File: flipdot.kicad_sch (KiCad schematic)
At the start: 22 parts, among them J4 Conn_01x05_Pin, J8 Conn_01x05_Pin, Q1 FDN338P

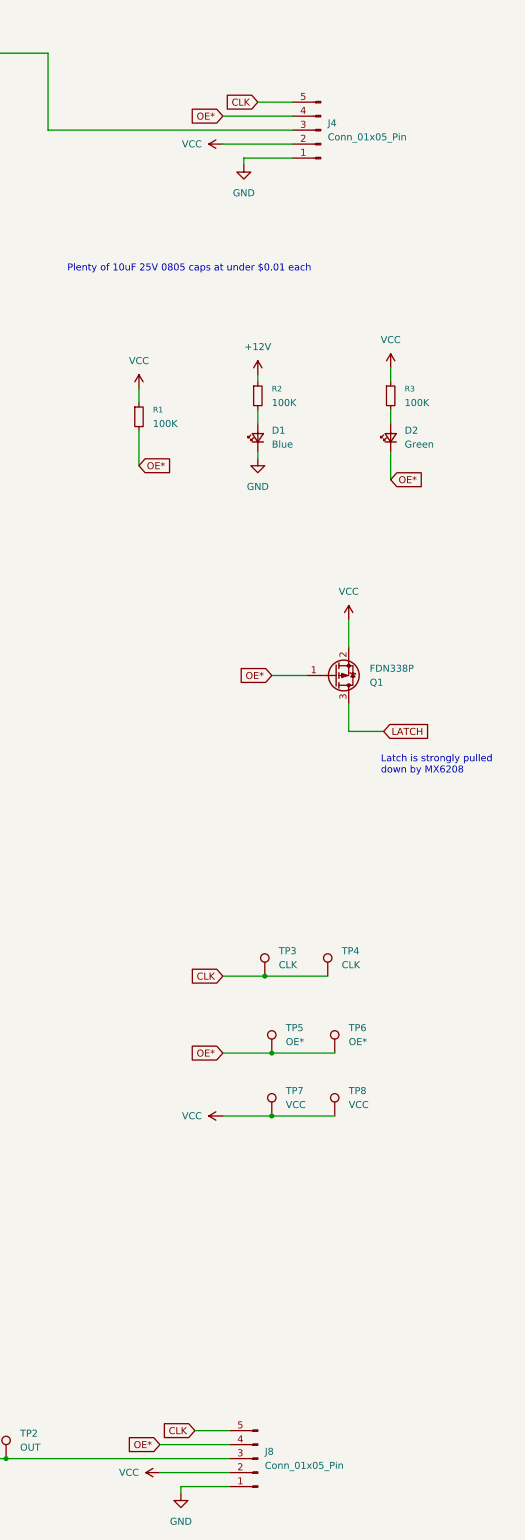
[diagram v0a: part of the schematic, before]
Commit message: add 12v out with polyfuse
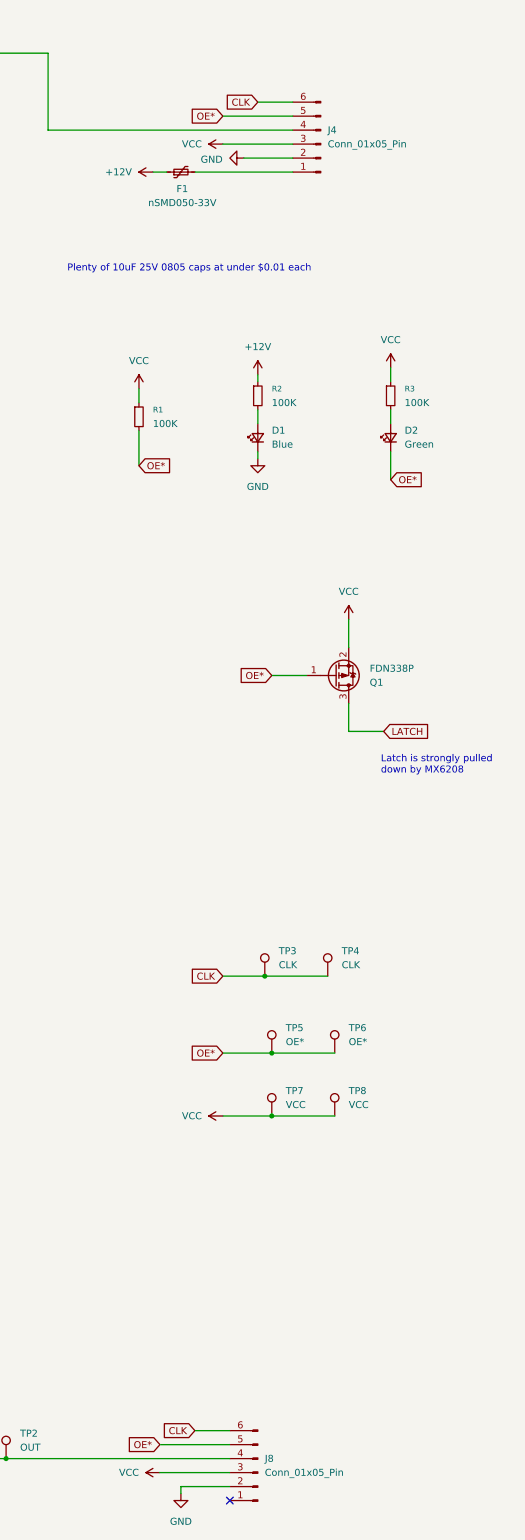
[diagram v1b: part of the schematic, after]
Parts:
- added F1: nSMD050-33V, Fuse:Fuse_1206_3216Metric, symbol Device:Polyfuse_Small
- J4, J8: footprint Connector_JST:JST_ZH_B5B-ZR_1x05_P1.50mm_Vertical -> Connector_JST:JST_ZH_B6B-ZR_1x06_P1.50mm_Vertical; symbol Connector:Conn_01x05_Pin -> Connector:Conn_01x06_Pin
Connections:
- net +12V: now also F1.1
- net CLK: now also J4.6 (Pin_6), J8.6 (Pin_6); no longer J4.5 (Pin_5), J8.5 (Pin_5)
- net GND: now also J4.2 (Pin_2), J8.2 (Pin_2); no longer J4.1 (Pin_1), J8.1 (Pin_1)
- net OE*: now also J4.5 (Pin_5), J8.5 (Pin_5); no longer J4.4 (Pin_4), J8.4 (Pin_4)
- net VCC: now also J4.3 (Pin_3), J8.3 (Pin_3); no longer J4.2 (Pin_2), J8.2 (Pin_2)
- net row1/DATA_IN: now also J4.4 (Pin_4); no longer J4.3 (Pin_3)
- net row13/DATA_OUT: now also J8.4 (Pin_4); no longer J8.3 (Pin_3)
- new net: F1.2, J4.1 (Pin_1)
- no-connect marks 0 -> 1
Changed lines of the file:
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@@
 		(color 0 0 0 0)
 	)
+	(no_connect
+		(at 146.05 287.02)
+	)
 	(wire
 		(pts
@@
 	(wire
 		(pts
+			(xy 132.08 45.72) (xy 134.62 45.72)
+		)
+		(stroke
+			(width 0)
+			(type default)
+		)
+	)
+	(wire
+		(pts
 			(xy 173.99 147.32) (xy 167.64 147.32)
 		)
@@
 	(wire
 		(pts
+			(xy 139.7 45.72) (xy 157.48 45.72)
+		)
+		(stroke
+			(width 0)
+			(type default)
+		)
+	)
+	(wire
+		(pts
 			(xy 43.18 248.92) (xy 43.18 259.08)
 		)
@@
 	(wire
 		(pts
-			(xy 148.59 44.45) (xy 148.59 43.18)
-		)
-		(stroke
-			(width 0)
-			(type default)
-		)
-	)
-	(wire
-		(pts
 			(xy 43.18 218.44) (xy 48.26 218.44)
 		)
@@
 	)
 	(symbol
-		(lib_id "Connector:Conn_01x05_Pin")
-		(at 162.56 38.1 180)
+		(lib_id "Device:Polyfuse_Small")
+		(at 137.16 45.72 90)
+		(unit 1)
+		(body_style 1)
+		(exclude_from_sim no)
+		(in_bom yes)
+		(on_board yes)
+		(in_pos_files yes)
+		(dnp no)
+		(property "Reference" "F1"
+			(at 137.414 48.768 90)
+			(show_name no)
+			(do_not_autoplace no)
+			(effects
+				(font
+					(size 1.27 1.27)
+				)
+			)
+		)
+		(property "Value" "nSMD050-33V"
+			(at 137.414 51.308 90)
+			(show_name no)
+			(do_not_autoplace no)
+			(effects
+				(font
+					(size 1.27 1.27)
+				)
+			)
+		)
+		(property "Footprint" "Fuse:Fuse_1206_3216Metric"
+			(at 142.24 44.45 0)
+			(hide yes)
+			(show_name no)
+			(do_not_autoplace no)
+			(effects
+				(font
+					(size 1.27 1.27)
+				)
+				(justify left)
+			)
+		)
+		(property "Datasheet" ""
+			(at 137.16 45.72 0)
+			(hide yes)
+			(show_name no)
+			(do_not_autoplace no)
+			(effects
+				(font
+					(size 1.27 1.27)
+				)
+			)
+		)
+		(property "Description" "Resettable fuse, polymeric positive temperature coefficient, small symbol"
+			(at 137.16 45.72 0)
+			(hide yes)
+			(show_name no)
+			(do_not_autoplace no)
+			(effects
+				(font
+					(size 1.27 1.27)
+				)
+			)
+		)
+		(pin "2"
+		)
+		(pin "1"
+		)
+		(instances
+			(project "flipdot"
+				(path "/2f7734fa-ef95-48ac-9211-21614044c9f8"
+					(reference "F1")
+					(unit 1)
+				)
+			)
+		)
+	)
+	(symbol
+		(lib_id "power:+12V")
+		(at 132.08 45.72 90)
+		(unit 1)
+		(body_style 1)
+		(exclude_from_sim no)
+		(in_bom yes)
+		(on_board yes)
+		(in_pos_files yes)
+		(dnp no)
+		(fields_autoplaced yes)
+		(property "Reference" "#PWR0561"
+			(at 135.89 45.72 0)
+			(hide yes)
+			(show_name no)
+			(do_not_autoplace no)
+			(effects
+				(font
+					(size 1.27 1.27)
+				)
+			)
+		)
+		(property "Value" "+12V"
+			(at 128.27 45.7199 90)
+			(show_name no)
+			(do_not_autoplace no)
+			(effects
+				(font
+					(size 1.27 1.27)
+				)
+				(justify left)
+			)
+		)
+		(property "Footprint" ""
+			(at 132.08 45.72 0)
+			(hide yes)
+			(show_name no)
+			(do_not_autoplace no)
+			(effects
+				(font
+					(size 1.27 1.27)
+				)
+			)
+		)
+		(property "Datasheet" ""
+			(at 132.08 45.72 0)
+			(hide yes)
+			(show_name no)
+			(do_not_autoplace no)
+			(effects
+				(font
+					(size 1.27 1.27)
+				)
+			)
+		)
+		(property "Description" "Power symbol creates a global label with name \"+12V\""
+			(at 132.08 45.72 0)
+			(hide yes)
+			(show_name no)
+			(do_not_autoplace no)
+			(effects
+				(font
+					(size 1.27 1.27)
+				)
+			)
+		)
+		(pin "1"
+		)
+		(instances
+			(project "flipdot"
+				(path "/2f7734fa-ef95-48ac-9211-21614044c9f8"
+					(reference "#PWR0561")
+					(unit 1)
+				)
+			)
+		)
+	)
+	(symbol
+		(lib_id "Connector:Conn_01x06_Pin")
+		(at 162.56 40.64 180)
 		(unit 1)
 		(body_style 1)
@@
 		(fields_autoplaced yes)
 		(property "Reference" "J4"
-			(at 163.83 36.8299 0)
+			(at 163.83 38.0999 0)
 			(show_name no)
 			(do_not_autoplace no)
@@
 		)
 		(property "Value" "Conn_01x05_Pin"
-			(at 163.83 39.3699 0)
+			(at 163.83 40.6399 0)
 			(show_name no)
 			(do_not_autoplace no)
@@
 			)
 		)
-		(property "Footprint" "Connector_JST:JST_ZH_B5B-ZR_1x05_P1.50mm_Vertical"
-			(at 162.56 38.1 0)
+		(property "Footprint" "Connector_JST:JST_ZH_B6B-ZR_1x06_P1.50mm_Vertical"
+			(at 162.56 40.64 0)
 			(hide yes)
 			(show_name no)
@@
 		)
 		(property "Datasheet" ""
-			(at 162.56 38.1 0)
+			(at 162.56 40.64 0)
 			(hide yes)
 			(show_name no)
@@
 			)
 		)
-		(property "Description" "Generic connector, single row, 01x05, script generated"
-			(at 162.56 38.1 0)
+		(property "Description" "Generic connector, single row, 01x06, script generated"
+			(at 162.56 40.64 0)
 			(hide yes)
 			(show_name no)
@@
 		)
 		(property "KiLib_Generator" "connector/JST"
-			(at 162.56 38.1 0)
+			(at 162.56 40.64 0)
 			(hide yes)
 			(show_name no)
@@
 		(pin "1"
 		)
+		(pin "6"
+		)
 		(instances
 			(project "flipdot"
@@
 	)
 	(symbol
-		(lib_id "Connector:Conn_01x05_Pin")
-		(at 151.13 279.4 180)
+		(lib_id "Connector:Conn_01x06_Pin")
+		(at 151.13 281.94 180)
 		(unit 1)
 		(body_style 1)
@@
 		(fields_autoplaced yes)
 		(property "Reference" "J8"
-			(at 152.4 278.1299 0)
+			(at 152.4 279.3999 0)
 			(show_name no)
 			(do_not_autoplace no)
@@
 		)
 		(property "Value" "Conn_01x05_Pin"
-			(at 152.4 280.6699 0)
+			(at 152.4 281.9399 0)
 			(show_name no)
 			(do_not_autoplace no)
@@
 			)
 		)
-		(property "Footprint" "Connector_JST:JST_ZH_B5B-ZR_1x05_P1.50mm_Vertical"
-			(at 151.13 279.4 0)
+		(property "Footprint" "Connector_JST:JST_ZH_B6B-ZR_1x06_P1.50mm_Vertical"
+			(at 151.13 281.94 0)
 			(hide yes)
 			(show_name no)
@@
 		)
 		(property "Datasheet" ""
-			(at 151.13 279.4 0)
+			(at 151.13 281.94 0)
 			(hide yes)
 			(show_name no)
@@
 			)
 		)
-		(property "Description" "Generic connector, single row, 01x05, script generated"
-			(at 151.13 279.4 0)
+		(property "Description" "Generic connector, single row, 01x06, script generated"
+			(at 151.13 281.94 0)
 			(hide yes)
 			(show_name no)
@@
 		)
 		(property "KiLib_Generator" "connector/JST"
-			(at 151.13 279.4 0)
+			(at 151.13 281.94 0)
 			(hide yes)
 			(show_name no)
@@
 		(pin "1"
 		)
+		(pin "6"
+		)
 		(instances
 			(project "flipdot"
@@
 	(symbol
 		(lib_id "power:GND")
-		(at 148.59 44.45 0)
+		(at 148.59 43.18 270)
 		(unit 1)
 		(body_style 1)
@@
 		(in_pos_files yes)
 		(dnp no)
-		(fields_autoplaced yes)
 		(property "Reference" "#PWR0554"
-			(at 148.59 50.8 0)
+			(at 142.24 43.18 0)
 			(hide yes)
 			(show_name no)
@@
 		)
 		(property "Value" "GND"
-			(at 148.59 49.53 0)
+			(at 142.748 43.434 90)
 			(show_name no)
 			(do_not_autoplace no)
@@
 		)
 		(property "Footprint" ""
-			(at 148.59 44.45 0)
+			(at 148.59 43.18 0)
 			(hide yes)
 			(show_name no)
@@
 		)
 		(property "Datasheet" ""
-			(at 148.59 44.45 0)
+			(at 148.59 43.18 0)
 			(hide yes)
 			(show_name no)
@@
 		)
 		(property "Description" "Power symbol creates a global label with name \"GND\" , ground"
-			(at 148.59 44.45 0)
+			(at 148.59 43.18 0)
 			(hide yes)
 			(show_name no)

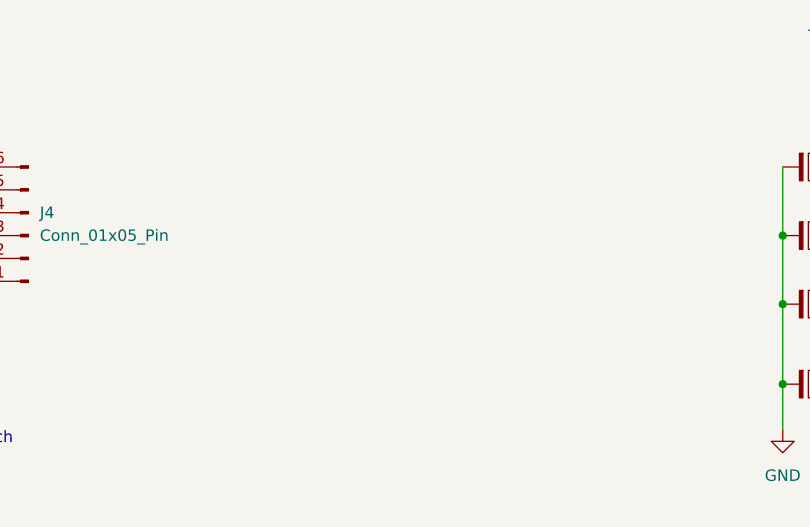
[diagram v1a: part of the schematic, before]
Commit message: add regulator after all
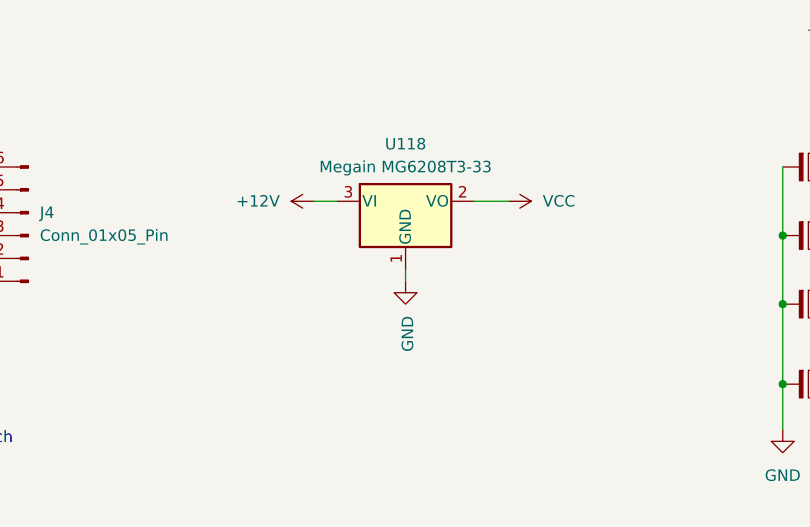
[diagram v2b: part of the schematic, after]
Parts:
- added U118: Megain MG6208T3-33, Package_TO_SOT_SMD:SOT-23, symbol Regulator_Linear:MCP1700x-330xxTT
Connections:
- net +12V: now also U118.3 (VI)
- net GND: now also U118.1 (GND)
- net VCC: now also U118.2 (VO)

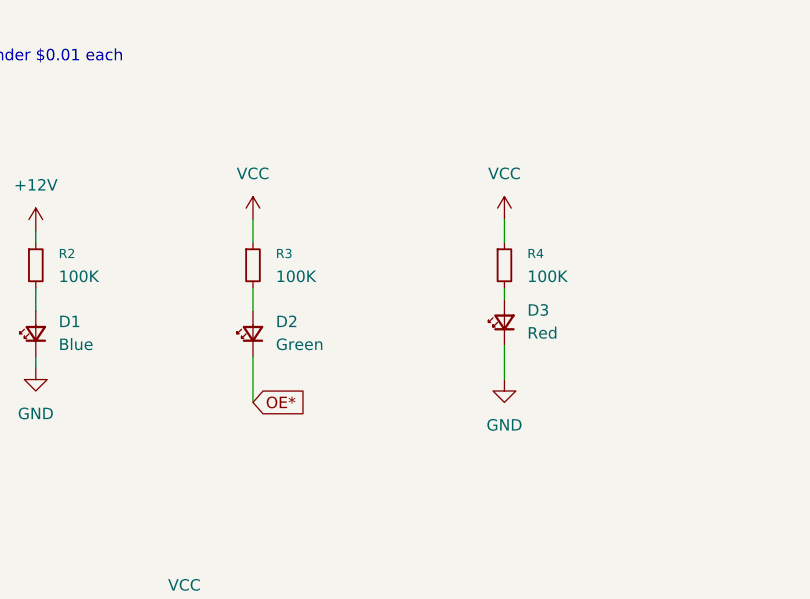
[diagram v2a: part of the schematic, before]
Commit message: remove unused LEDs
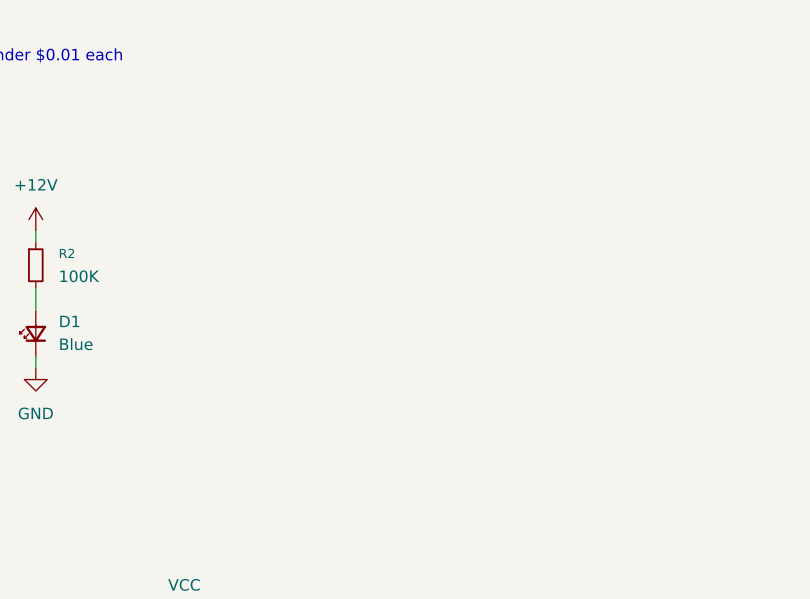
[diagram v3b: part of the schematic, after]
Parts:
- removed D2: Green, LED_SMD:LED_0603_1608Metric, symbol Device:LED_Small
- removed D3: Red, LED_SMD:LED_0603_1608Metric, symbol Device:LED_Small
- removed R3, R4: 100K, Resistor_SMD:R_0603_1608Metric, symbol Device:R_Small
